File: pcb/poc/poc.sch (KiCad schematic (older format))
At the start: 59 parts, among them J1 USB_B_Mini, J2 Right, J3 Left, J4 AVR-ISP-6, J5 Conn_02x11_Odd_Even, J6 Conn_02x06_Odd_Even, SW1 SW_Push, SW10 SW_Push_45deg, SW11 SW_Push_45deg, SW2 SW_Push_45deg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

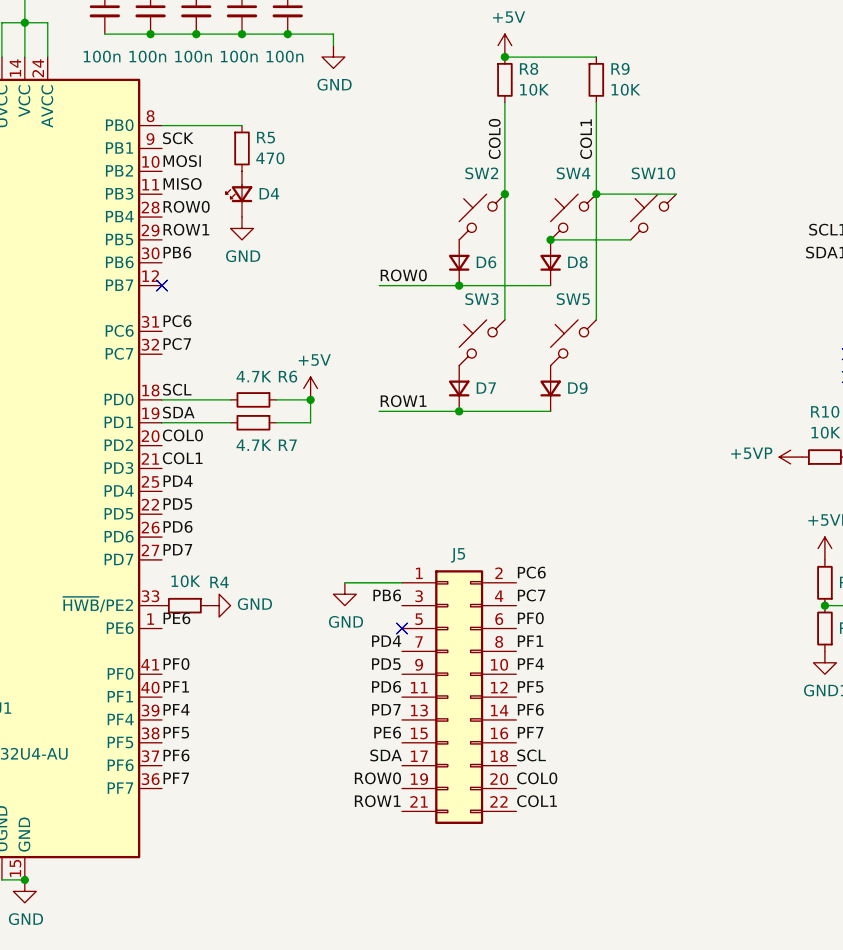
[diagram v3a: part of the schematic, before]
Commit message: pcb: poc: Routed buttons and breakout
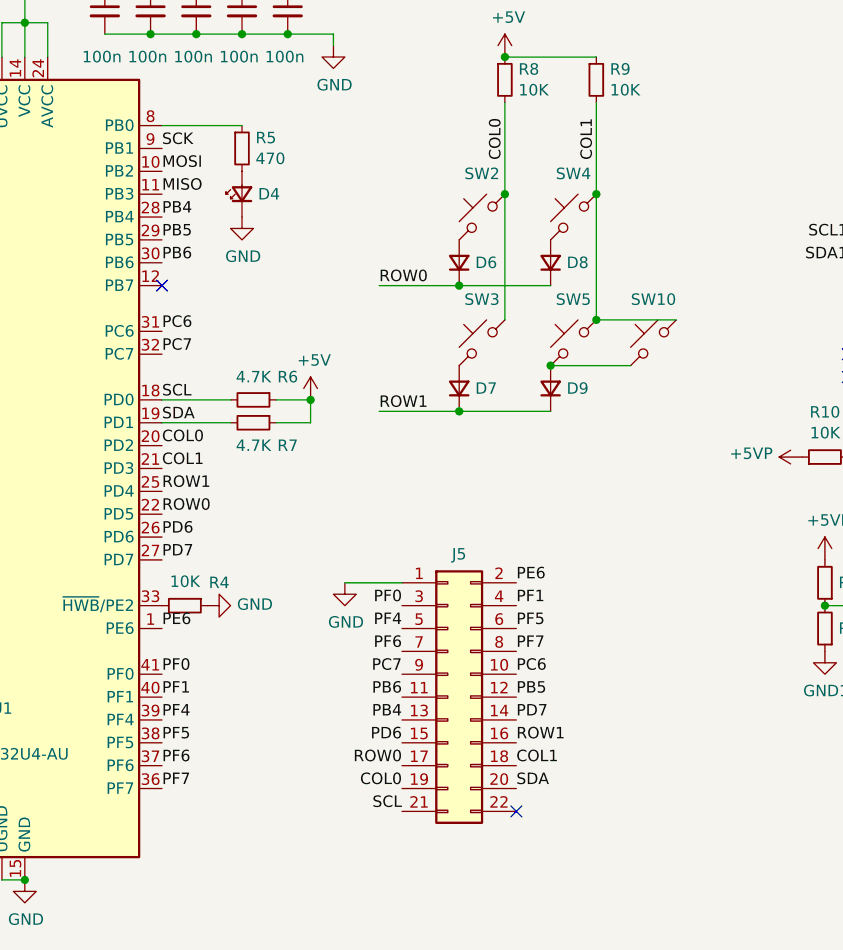
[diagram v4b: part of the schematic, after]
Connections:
- net COL0: now also J5.19 (Pin_19); no longer J5.20 (Pin_20)
- net COL1: now also J5.18 (Pin_18); no longer J5.22 (Pin_22)
- net PB6: now also J5.11 (Pin_11); no longer J5.3 (Pin_3)
- net PC6: now also J5.10 (Pin_10); no longer J5.2 (Pin_2)
- net PC7: now also J5.9 (Pin_9); no longer J5.4 (Pin_4)
- net PD6: now also J5.15 (Pin_15); no longer J5.11 (Pin_11)
- net PD7: now also J5.14 (Pin_14); no longer J5.13 (Pin_13)
- net PE6: now also J5.2 (Pin_2); no longer J5.15 (Pin_15)
- net PF0: now also J5.3 (Pin_3); no longer J5.6 (Pin_6)
- net PF1: now also J5.4 (Pin_4); no longer J5.8 (Pin_8)
- net PF4: now also J5.5 (Pin_5); no longer J5.10 (Pin_10)
- net PF5: now also J5.6 (Pin_6); no longer J5.12 (Pin_12)
- net PF6: now also J5.7 (Pin_7); no longer J5.14 (Pin_14)
- net PF7: now also J5.8 (Pin_8); no longer J5.16 (Pin_16)
- net ROW0: now also J5.17 (Pin_17), U1.22 (PD5); no longer J5.19 (Pin_19), U1.28 (PB4)
- net ROW1: now also J5.16 (Pin_16), U1.25 (PD4); no longer J5.21 (Pin_21), U1.29 (PB5)
- net SCL: now also J5.21 (Pin_21); no longer J5.18 (Pin_18)
- net SDA: now also J5.20 (Pin_20); no longer J5.17 (Pin_17)
- net at D8.2 (A), SW4.2: no longer SW10.2
- net at D9.2 (A), SW5.2: now also SW10.2
- removed net PD4: J5.7 (Pin_7), U1.25 (PD4)
- removed net PD5: J5.9 (Pin_9), U1.22 (PD5)
- new net PB4: J5.13 (Pin_13), U1.28 (PB4)
- new net PB5: J5.12 (Pin_12), U1.29 (PB5)
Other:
- moved on the sheet: SW10
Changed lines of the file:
@@
 Wire Wire Line
 	5550 4250 5950 4250
-Text Label 4250 3400 0    50   ~ 0
+Text Label 4250 4700 0    50   ~ 0
 ROW0
-Text Label 4250 3500 0    50   ~ 0
+Text Label 4250 4600 0    50   ~ 0
 ROW1
 Text Label 4250 4400 0    50   ~ 0
@@
 Text Label 4250 4000 0    50   ~ 0
 PC7
-Text Label 4250 4600 0    50   ~ 0
-PD4
-Text Label 4250 4700 0    50   ~ 0
-PD5
 Text Label 4250 4800 0    50   ~ 0
 PD6
@@
 Text Label 4250 5900 0    50   ~ 0
 PF7
-Text Label 5800 5700 0    50   ~ 0
-PF7
-Text Label 5800 5600 0    50   ~ 0
-PF6
-Text Label 5800 5500 0    50   ~ 0
-PF5
-Text Label 5800 5400 0    50   ~ 0
-PF4
-Text Label 5800 5300 0    50   ~ 0
-PF1
-Text Label 5800 5200 0    50   ~ 0
-PF0
-Text Label 5300 5700 2    50   ~ 0
-PE6
-Text Label 5300 5600 2    50   ~ 0
-PD7
-Text Label 5300 5500 2    50   ~ 0
-PD6
-Text Label 5300 5400 2    50   ~ 0
-PD5
-Text Label 5300 5300 2    50   ~ 0
-PD4
-Text Label 5800 5100 0    50   ~ 0
-PC7
-Text Label 5800 5000 0    50   ~ 0
-PC6
-Text Label 5300 5100 2    50   ~ 0
-PB6
 $Comp
 L power:GND #PWR025
@@
 L Switch:SW_Push_45deg SW10
 U 1 1 60466D2C
-P 6400 3400
-F 0 "SW10" H 6400 3589 50  0000 C CNN
-F 1 "SW_Push_45deg" H 6400 3590 50  0001 C CNN
-F 2 "Button_Switch_Keyboard:SW_Cherry_MX_1.00u_PCB" H 6400 3400 50  0001 C CNN
-F 3 "~" H 6400 3400 50  0001 C CNN
-	1    6400 3400
+P 6400 3950
+F 0 "SW10" H 6400 4139 50  0000 C CNN
+F 1 "SW_Push_45deg" H 6400 4140 50  0001 C CNN
+F 2 "Button_Switch_Keyboard:SW_Cherry_MX_1.00u_PCB" H 6400 3950 50  0001 C CNN
+F 3 "~" H 6400 3950 50  0001 C CNN
+	1    6400 3950
 	-1   0    0    -1
 $EndComp
-Wire Wire Line
-	6150 3300 6500 3300
-Wire Wire Line
-	6300 3500 5950 3500
-Connection ~ 5950 3500
 $Comp
 L Switch:SW_Push_45deg SW11
@@
 	1    0    0    -1
 $EndComp
-Text Label 5800 5800 0    50   ~ 0
-SCL
-Text Label 5300 5800 2    50   ~ 0
-SDA
-Text Label 5800 5900 0    50   ~ 0
-COL0
-Text Label 5800 6000 0    50   ~ 0
-COL1
-Text Label 5300 5900 2    50   ~ 0
-ROW0
-Text Label 5300 6000 2    50   ~ 0
-ROW1
 $Comp
 L Connector_Generic:Conn_02x11_Odd_Even J5
@@
 D1-
 NoConn ~ 4250 3700
-NoConn ~ 5300 5200
+Wire Wire Line
+	6500 3850 6150 3850
+Connection ~ 6150 3850
+Wire Wire Line
+	6300 4050 5950 4050
+Connection ~ 5950 4050
+Text Label 4250 3400 0    50   ~ 0
+PB4
+Text Label 4250 3500 0    50   ~ 0
+PB5
+Text Label 5800 5000 0    50   ~ 0
+PE6
+Text Label 5300 5100 2    50   ~ 0
+PF0
+Text Label 5800 5100 0    50   ~ 0
+PF1
+Text Label 5300 5200 2    50   ~ 0
+PF4
+Text Label 5800 5200 0    50   ~ 0
+PF5
+Text Label 5300 5300 2    50   ~ 0
+PF6
+Text Label 5800 5300 0    50   ~ 0
+PF7
+Text Label 5300 5400 2    50   ~ 0
+PC7
+Text Label 5800 5400 0    50   ~ 0
+PC6
+Text Label 5300 5500 2    50   ~ 0
+PB6
+Text Label 5800 5500 0    50   ~ 0
+PB5
+Text Label 5300 5600 2    50   ~ 0
+PB4
+Text Label 5800 5600 0    50   ~ 0
+PD7
+Text Label 5300 5700 2    50   ~ 0
+PD6
+Text Label 5800 5700 0    50   ~ 0
+ROW1
+Text Label 5300 5800 2    50   ~ 0
+ROW0
+Text Label 5800 5800 0    50   ~ 0
+COL1
+Text Label 5300 5900 2    50   ~ 0
+COL0
+Text Label 5800 5900 0    50   ~ 0
+SDA
+Text Label 5300 6000 2    50   ~ 0
+SCL
+NoConn ~ 5800 6000
 $EndSCHEMATC

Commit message: pcb: poc: Change 2x11 to 2x10 breakout
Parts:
- J5: value Conn_02x11_Odd_Even -> Conn_02x10_Odd_Even; footprint Connector_PinSocket_2.54mm:PinSocket_2x11_P2.54mm_Vertical -> Connector_PinSocket_2.54mm:PinSocket_2x10_P2.54mm_Vertical; symbol Connector_Generic:Conn_02x11_Odd_Even -> Connector_Generic:Conn_02x10_Odd_Even
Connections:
- net SCL: no longer J5.21 (Pin_21)
- net SDA: no longer J5.20 (Pin_20)
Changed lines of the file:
@@
 $EndComp
 $Comp
-L Connector_Generic:Conn_02x11_Odd_Even J5
+L Connector_Generic:Conn_02x10_Odd_Even J5
 U 1 1 604C9372
-P 5500 5500
-F 0 "J5" H 5550 6125 50  0000 C CNN
-F 1 "Conn_02x11_Odd_Even" H 5550 6126 50  0001 C CNN
-F 2 "Connector_PinSocket_2.54mm:PinSocket_2x11_P2.54mm_Vertical" H 5500 5500 50  0001 C CNN
-F 3 "~" H 5500 5500 50  0001 C CNN
-	1    5500 5500
+P 5500 5400
+F 0 "J5" H 5550 6025 50  0000 C CNN
+F 1 "Conn_02x10_Odd_Even" H 5550 6026 50  0001 C CNN
+F 2 "Connector_PinSocket_2.54mm:PinSocket_2x10_P2.54mm_Vertical" H 5500 5400 50  0001 C CNN
+F 3 "~" H 5500 5400 50  0001 C CNN
+	1    5500 5400
 	1    0    0    -1
 $EndComp
@@
 Text Label 5300 5900 2    50   ~ 0
 COL0
-Text Label 5800 5900 0    50   ~ 0
-SDA
-Text Label 5300 6000 2    50   ~ 0
-SCL
-NoConn ~ 5800 6000
+NoConn ~ 5800 5900
 $EndSCHEMATC

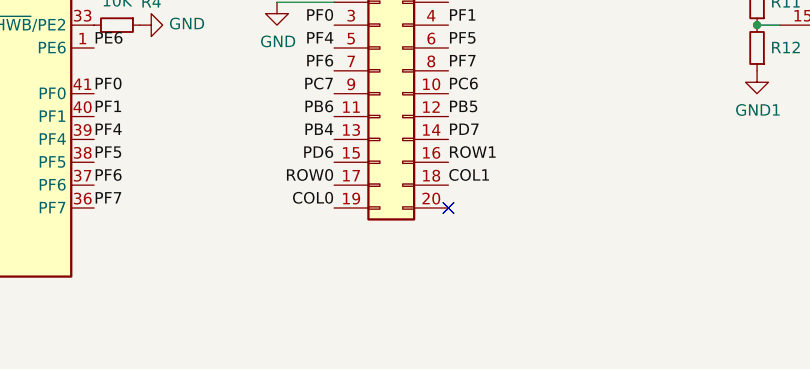
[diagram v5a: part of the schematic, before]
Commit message: pcb: poc: i2c breakout and crystal ground
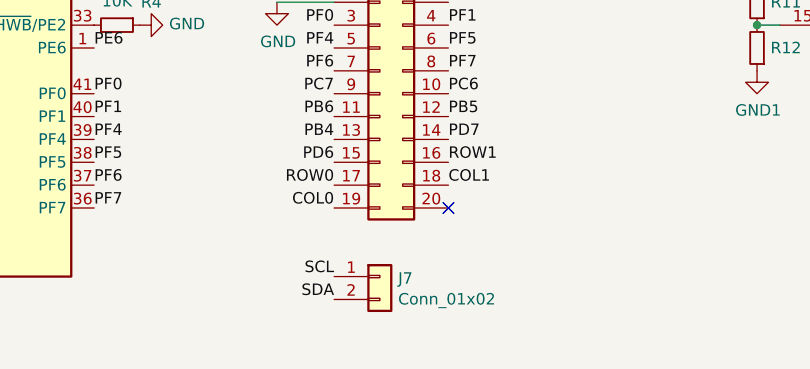
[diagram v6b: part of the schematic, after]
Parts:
- added J7: Conn_01x02, Connector_PinHeader_2.54mm:PinHeader_1x02_P2.54mm_Vertical, symbol Connector_Generic:Conn_01x02
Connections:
- net SCL: now also J7.1 (Pin_1)
- net SDA: now also J7.2 (Pin_2)
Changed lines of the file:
@@
 COL0
 NoConn ~ 5800 5900
+$Comp
+L Connector_Generic:Conn_01x02 J7
+U 1 1 606762A5
+P 5500 6200
+F 0 "J7" H 5580 6192 50  0000 L CNN
+F 1 "Conn_01x02" H 5580 6101 50  0000 L CNN
+F 2 "Connector_PinHeader_2.54mm:PinHeader_1x02_P2.54mm_Vertical" H 5500 6200 50  0001 C CNN
+F 3 "~" H 5500 6200 50  0001 C CNN
+	1    5500 6200
+	1    0    0    -1
+$EndComp
+Text Label 5300 6200 2    50   ~ 0
+SCL
+Text Label 5300 6300 2    50   ~ 0
+SDA
 $EndSCHEMATC

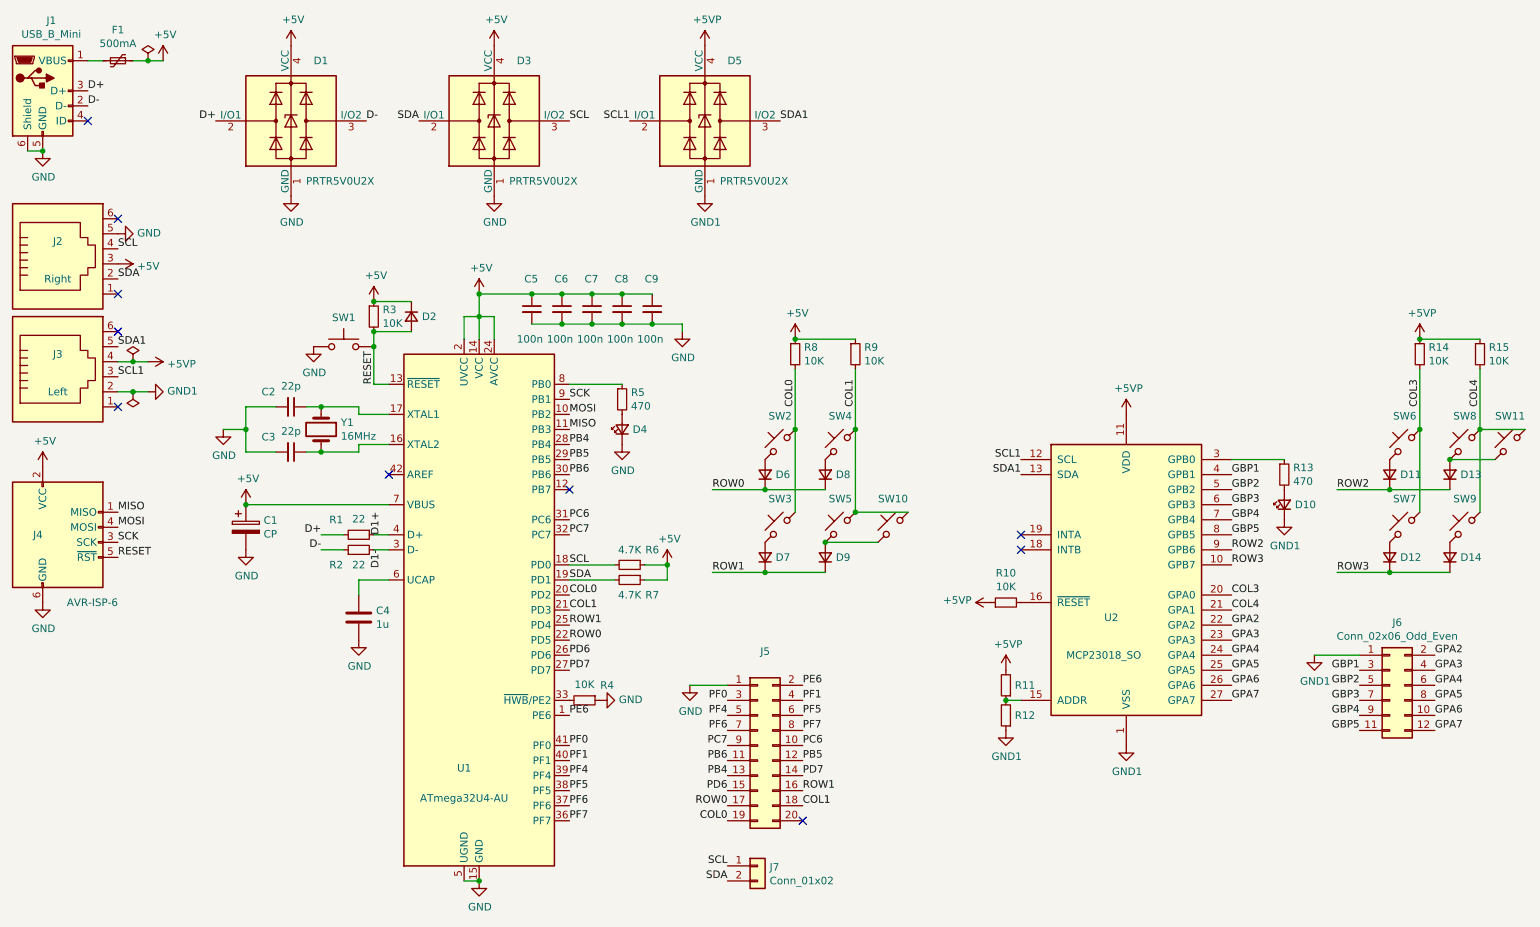
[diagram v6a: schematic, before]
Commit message: pcb: poc: MCP side layout
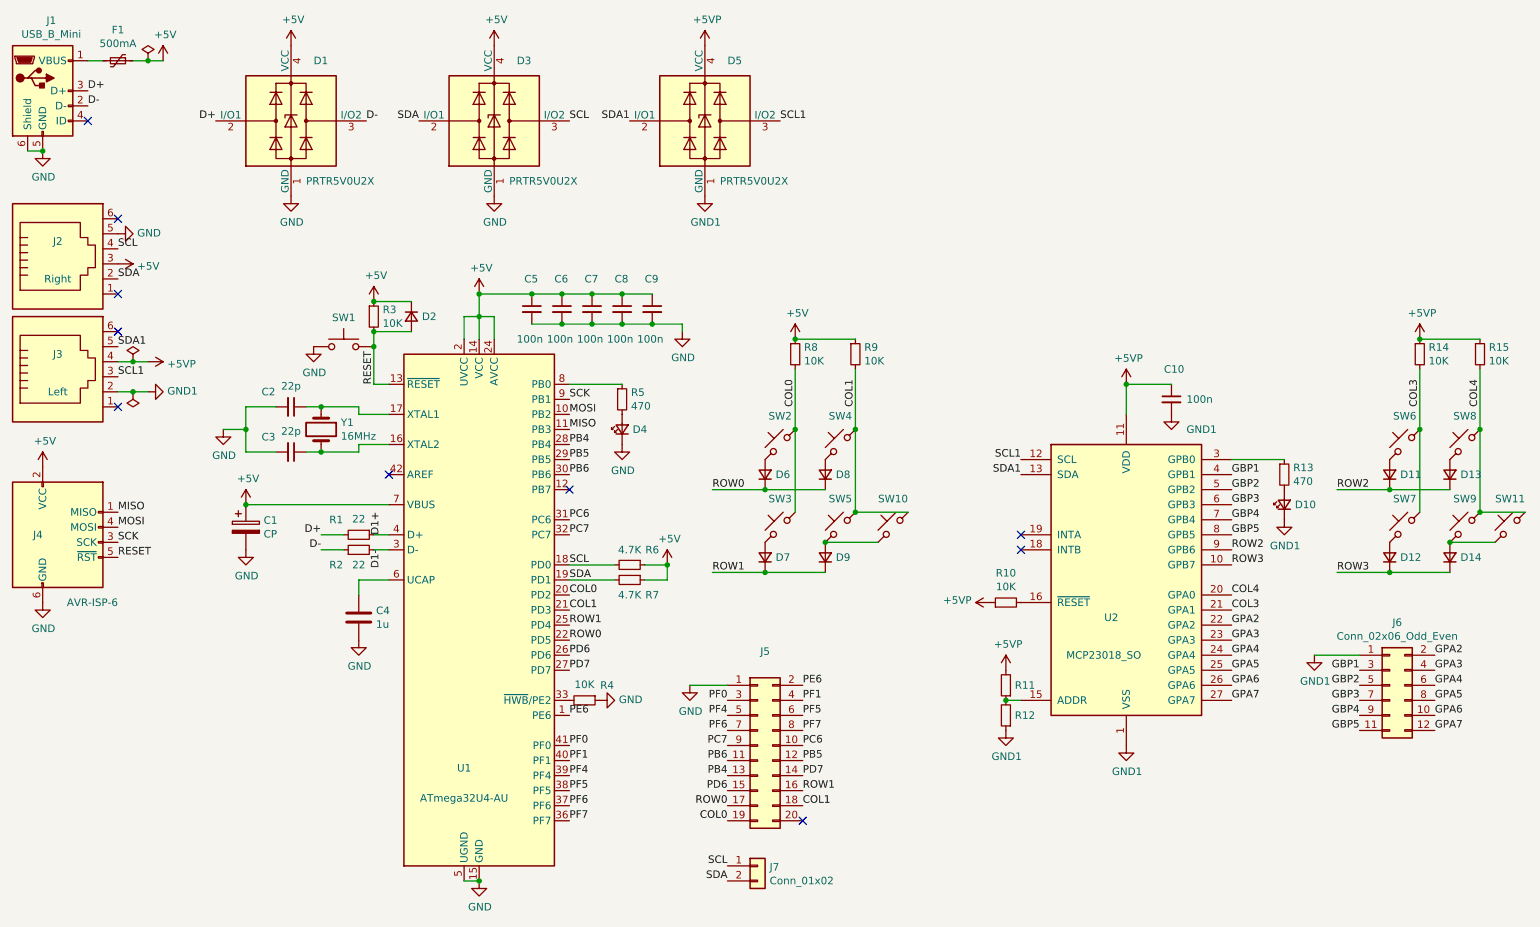
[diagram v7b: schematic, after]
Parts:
- added C10: 100n, Capacitor_SMD:C_0805_2012Metric_Pad1.18x1.45mm_HandSolder, symbol Device:C_Small
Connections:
- net +5VP: now also C10.1
- net COL3: now also U2.21 (GPA1); no longer U2.20 (GPA0)
- net COL4: now also U2.20 (GPA0); no longer U2.21 (GPA1)
- net GND1: now also C10.2
- net SCL1: now also D5.3 (I/O2); no longer D5.2 (I/O1)
- net SDA1: now also D5.2 (I/O1); no longer D5.3 (I/O2)
- net at D13.2 (A), SW8.2: no longer SW11.2
- net at D14.2 (A), SW9.2: now also SW11.2
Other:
- moved on the sheet: SW11
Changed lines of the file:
@@
 	1    0    0    -1
 $EndComp
-Text Label 4650 1250 2    50   ~ 0
-SCL1
-Text Label 5650 1250 0    50   ~ 0
-SDA1
 $Comp
 L power:GND1 #PWR033
@@
 L power:+5VP #PWR032
 U 1 1 606F4BB8
-P 7950 3200
-F 0 "#PWR032" H 7950 3050 50  0001 C CNN
-F 1 "+5VP" H 7965 3373 50  0000 C CNN
-F 2 "" H 7950 3200 50  0001 C CNN
-F 3 "" H 7950 3200 50  0001 C CNN
-	1    7950 3200
+P 7950 3000
+F 0 "#PWR032" H 7950 2850 50  0001 C CNN
+F 1 "+5VP" H 7965 3173 50  0000 C CNN
+F 2 "" H 7950 3000 50  0001 C CNN
+F 3 "" H 7950 3000 50  0001 C CNN
+	1    7950 3000
 	1    0    0    -1
 $EndComp
@@
 Text Label 8650 4200 0    50   ~ 0
 ROW3
+Text Label 8650 4500 0    50   ~ 0
+COL3
 Text Label 8650 4400 0    50   ~ 0
-COL3
-Text Label 8650 4500 0    50   ~ 0
 COL4
 $Comp
@@
 L Switch:SW_Push_45deg SW11
 U 1 1 6046FE50
-P 10500 3400
-F 0 "SW11" H 10500 3589 50  0000 C CNN
-F 1 "SW_Push_45deg" H 10500 3590 50  0001 C CNN
-F 2 "Button_Switch_Keyboard:SW_Cherry_MX_1.00u_PCB" H 10500 3400 50  0001 C CNN
-F 3 "~" H 10500 3400 50  0001 C CNN
-	1    10500 3400
+P 10500 3950
+F 0 "SW11" H 10500 4139 50  0000 C CNN
+F 1 "SW_Push_45deg" H 10500 4140 50  0001 C CNN
+F 2 "Button_Switch_Keyboard:SW_Cherry_MX_1.00u_PCB" H 10500 3950 50  0001 C CNN
+F 3 "~" H 10500 3950 50  0001 C CNN
+	1    10500 3950
 	-1   0    0    -1
 $EndComp
-Wire Wire Line
-	10600 3300 10300 3300
-Wire Wire Line
-	10400 3500 10100 3500
-Connection ~ 10100 3500
 $Comp
 L power:GND1 #PWR0101
@@
 Text Label 5300 6300 2    50   ~ 0
 SDA
+$Comp
+L Device:C_Small C10
+U 1 1 606987BF
+P 8250 3100
+F 0 "C10" H 8200 3300 50  0000 L CNN
+F 1 "100n" H 8350 3100 50  0000 L CNN
+F 2 "Capacitor_SMD:C_0805_2012Metric_Pad1.18x1.45mm_HandSolder" H 8250 3100 50  0001 C CNN
+F 3 "~" H 8250 3100 50  0001 C CNN
+	1    8250 3100
+	1    0    0    -1
+$EndComp
+Wire Wire Line
+	7950 3000 7950 3200
+Wire Wire Line
+	8250 3000 7950 3000
+Connection ~ 7950 3000
+$Comp
+L power:GND1 #PWR027
+U 1 1 606AD8E6
+P 8250 3200
+F 0 "#PWR027" H 8250 2950 50  0001 C CNN
+F 1 "GND1" H 8450 3100 50  0000 C CNN
+F 2 "" H 8250 3200 50  0001 C CNN
+F 3 "" H 8250 3200 50  0001 C CNN
+	1    8250 3200
+	1    0    0    -1
+$EndComp
+Text Label 4650 1250 2    50   ~ 0
+SDA1
+Text Label 5650 1250 0    50   ~ 0
+SCL1
+Wire Wire Line
+	10300 3850 10600 3850
+Connection ~ 10300 3850
+Wire Wire Line
+	10100 4050 10400 4050
+Connection ~ 10100 4050
 $EndSCHEMATC
